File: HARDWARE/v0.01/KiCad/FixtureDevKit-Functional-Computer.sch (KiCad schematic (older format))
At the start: 23 parts, among them J49 Conn_01x20, J50 Conn_01x20, J51 CHIP4RH, J52 Conn_01x35, J53 Conn_01x35, J54 Conn_01x20, J55 Conn_01x20, J56 CHIP4B2B, J57 CHIP4LH, J58 VBUS, J59 USB_A, J60 JST-2P, J61 Audio-Jack-3, SW9 SW_Push

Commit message: updating the cover page
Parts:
- added F?: 3A, symbol Fuse
- added SW?: On/Off, symbol SW_Push_SPDT
- added TP?: D+, symbol TEST
- added TP?: D-, symbol TEST
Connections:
- net USBOTG_B_DM: now also TP?.1
- net USBOTG_B_DP: now also TP?.1
- net C4-PWR-IN: now reaches J55.1 (Pin_1), J57.2 (CHG-IN)
- net C4-PWR-IN: now also J52.31 (Pin_31), J52.32 (Pin_32), J52.33 (Pin_33), J52.34 (Pin_34), J52.35 (Pin_35), J56.61 (USB_VBUS), J56.63 (USB_VBUS), J56.65 (USB_VBUS), J56.67 (USB_VBUS), J56.69 (USB_VBUS), SW?.3 (C)
- net at J51.2 (VCC-5V): no longer J50.1 (Pin_1)
- net I2C-SDA: now reaches J49.18 (Pin_18), J51.35 (GPIODV_28)
- net I2C-SDA: now also J52.29 (Pin_29), J56.57 (GPIODV_28)
- net I2C-SCK: now reaches J49.19 (Pin_19), J51.37 (GPIODV_29)
- net I2C-SCK: now also J52.30 (Pin_30), J56.59 (GPIODV_29)
- net STATUSLED renamed C4-VCC-3V3
- new net: F?.2, SW?.2 (B)
- new net +5V: F?.1
- new net C4-VCC-5V: J50.1 (Pin_1)
- no-connect marks 0 -> 1
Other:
- note added: "PWRSW"
- note added: "Sheet Connections"
- note removed: "TODO:\n- verify all pinouts\n- test points"
- moved on the sheet: J52, J53, J56

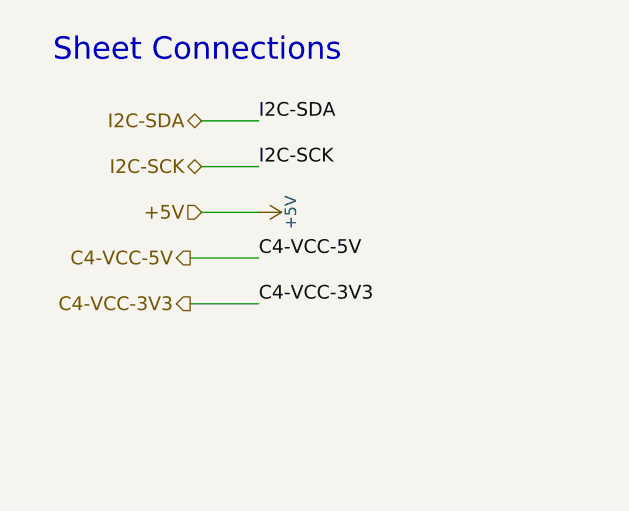
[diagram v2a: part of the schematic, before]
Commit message: adding labelings, hierarchy pins, and page titles
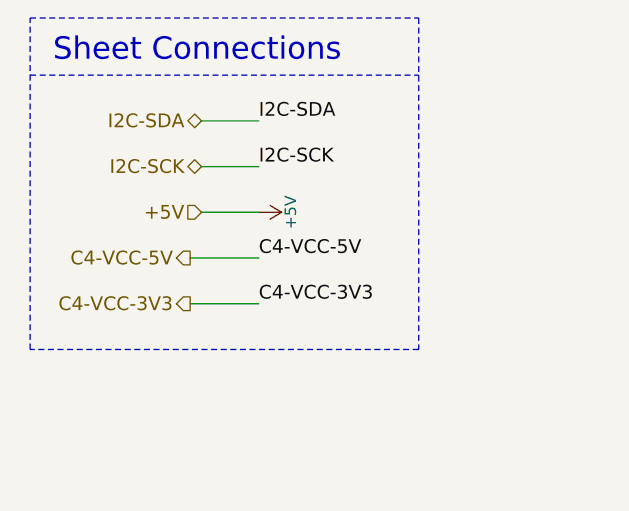
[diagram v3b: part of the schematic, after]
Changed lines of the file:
@@
 encoding utf-8
 Sheet 10 10
-Title ""
-Date ""
-Rev ""
-Comp ""
-Comment1 ""
+Title "CHIP4 Functional Computer"
+Date "2017-10-25"
+Rev "v0.01"
+Comp "Next Thing Co"
+Comment1 "Havin' a Blast!"
 Comment2 ""
 Comment3 ""
@@
 Wire Wire Line
 	9900 950  10100 950
+Wire Notes Line
+	500  500  2200 500
+Wire Notes Line
+	2200 500  2200 1950
+Wire Notes Line
+	2200 1950 500  1950
+Wire Notes Line
+	500  1950 500  500
+Wire Notes Line
+	500  750  2200 750
 $EndSCHEMATC

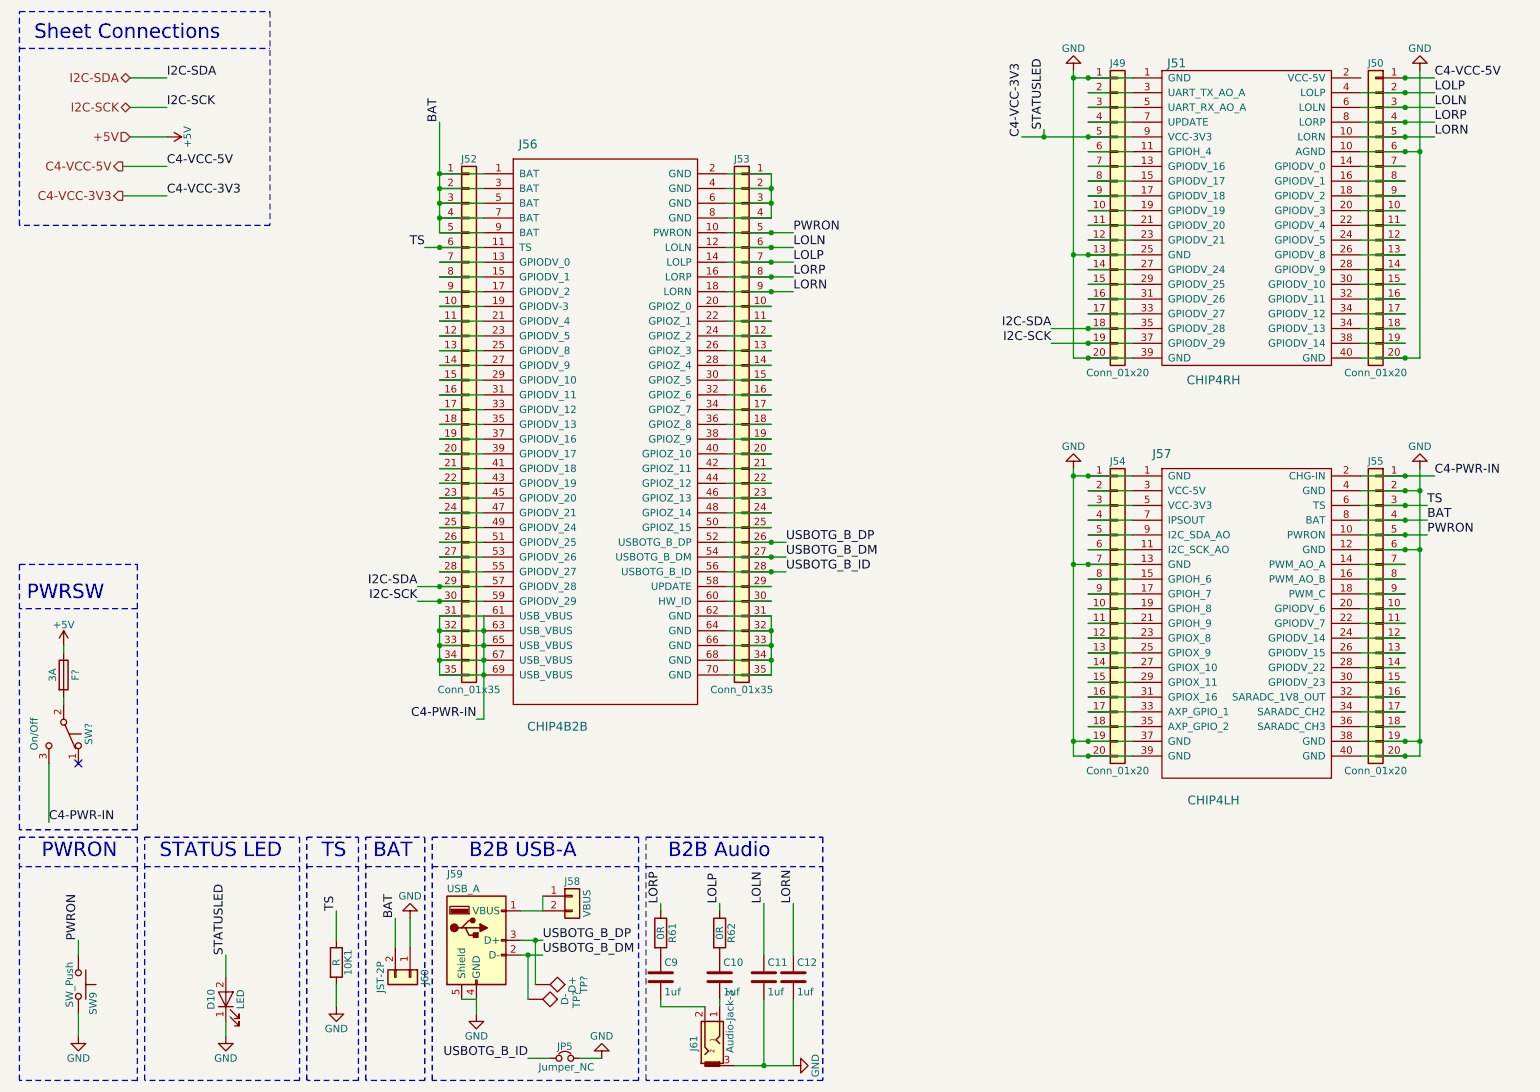
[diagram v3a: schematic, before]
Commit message: adjusting page sizes and cleaning up schematics
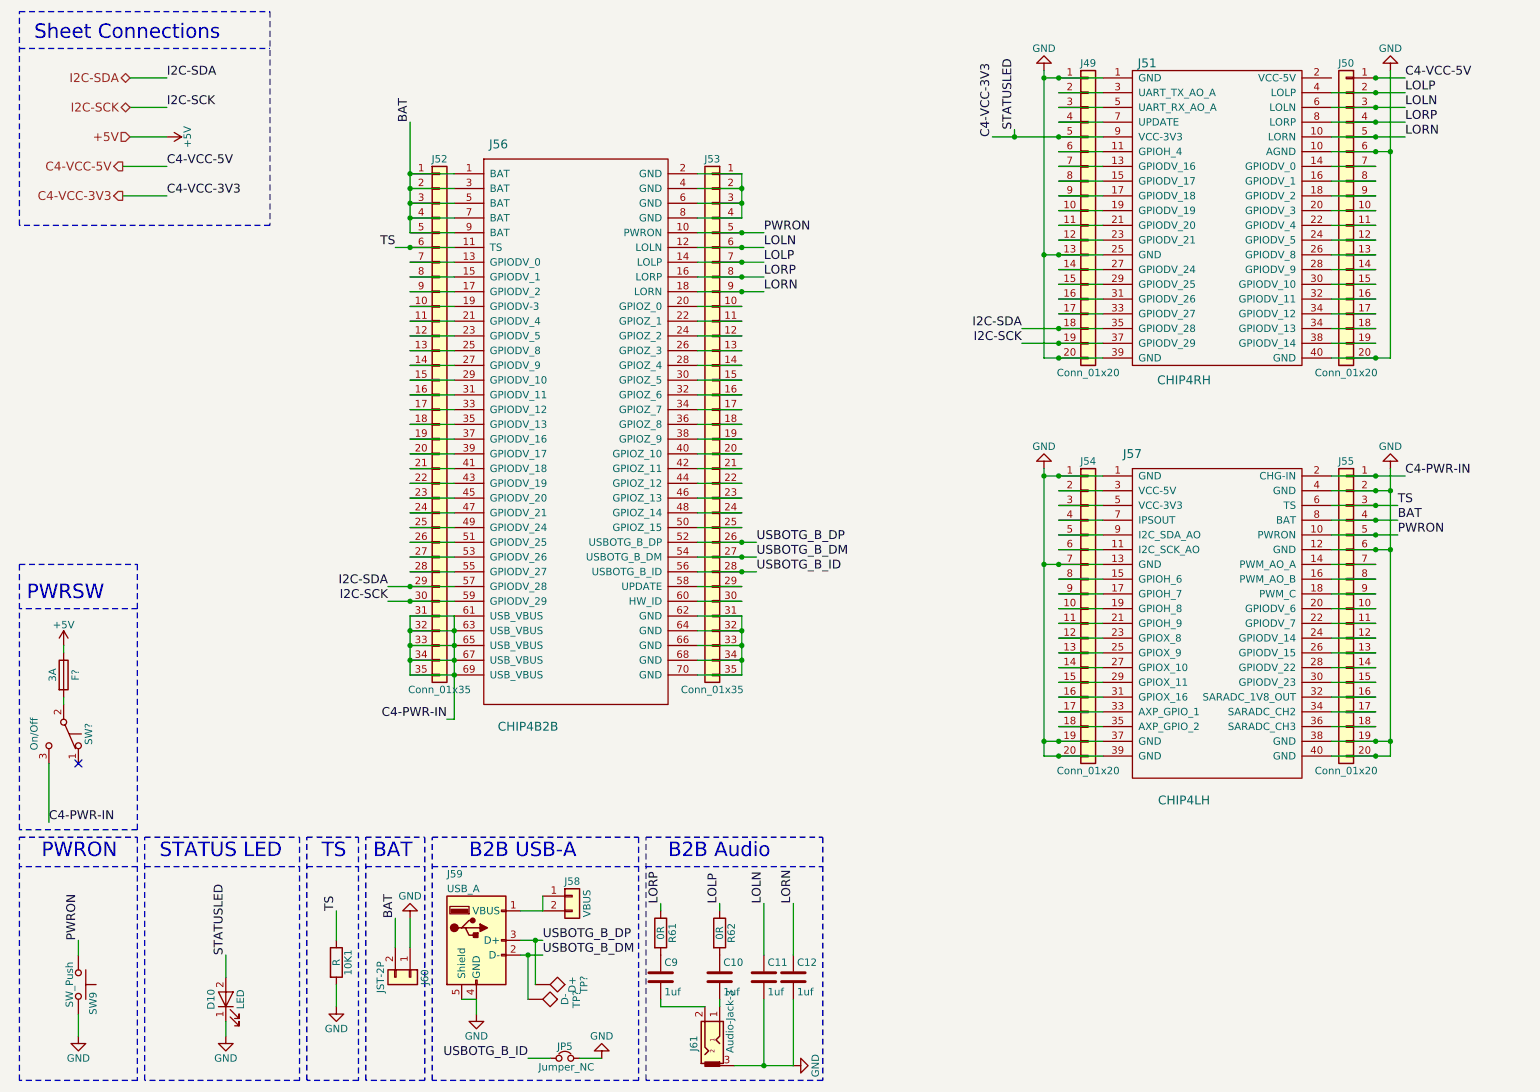
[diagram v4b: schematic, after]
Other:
- moved on the sheet: J49, J50, J51, J52, J53, J54, J55, J56, J57

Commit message: cleaning up schematic, run rules check, generate net list
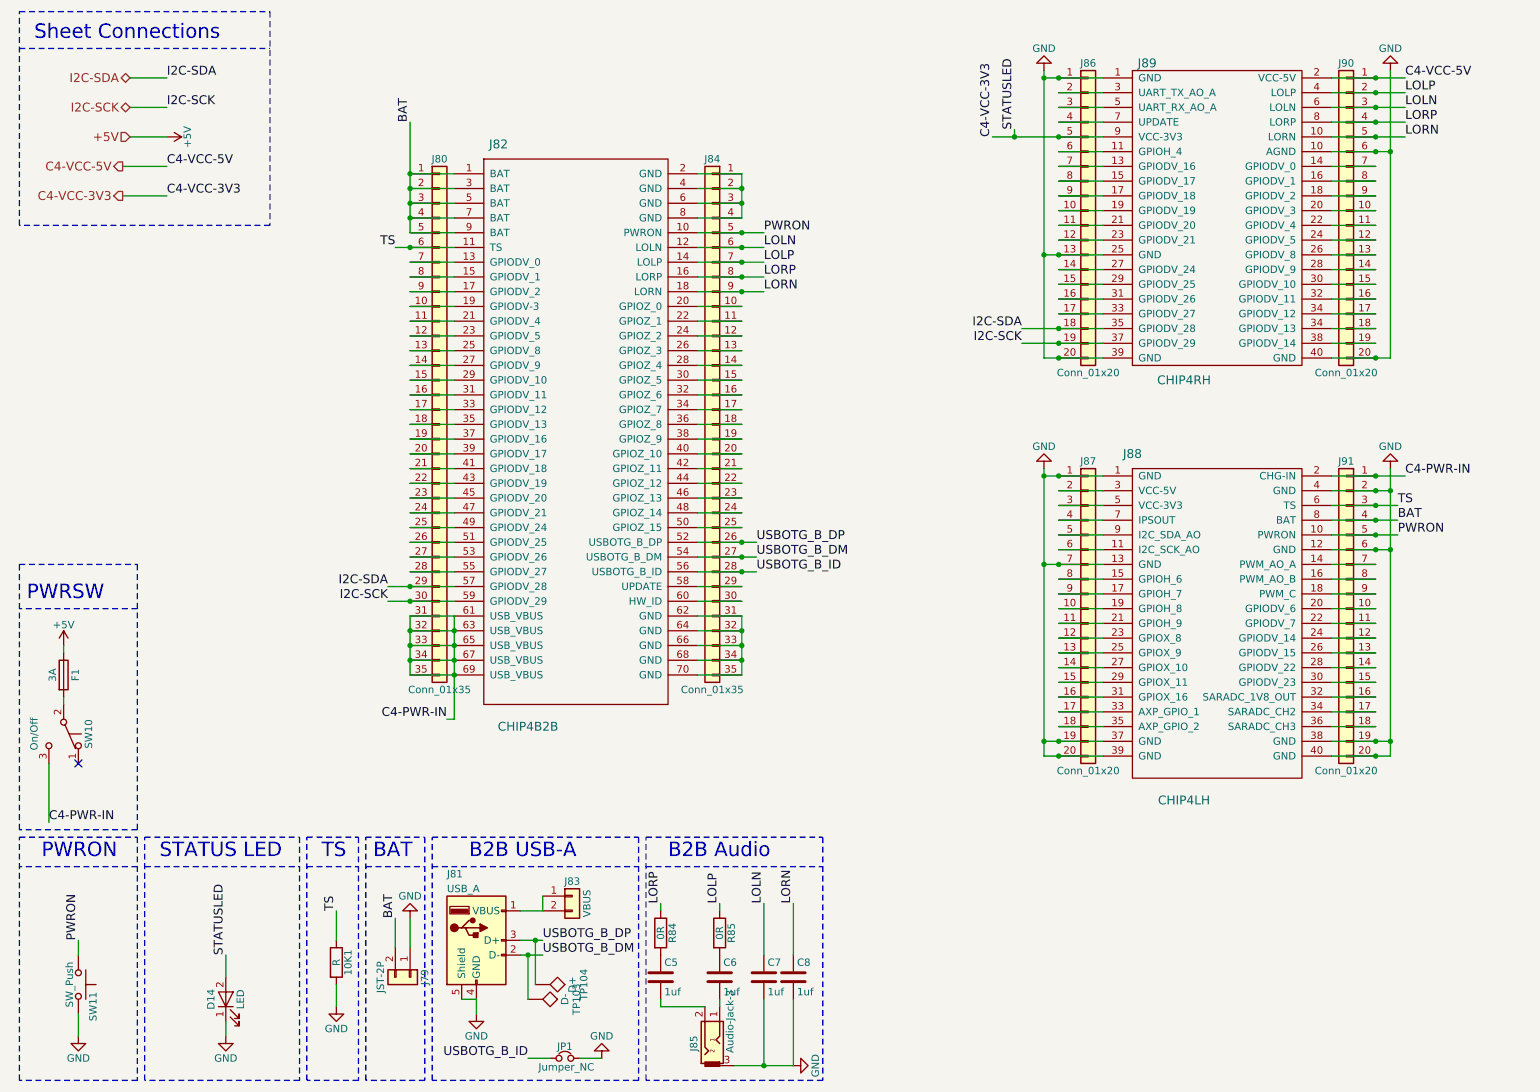
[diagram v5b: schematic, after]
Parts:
- gave numbers to parts that had none: 4
- renumbered C9 to C5, C10 to C6, C11 to C7, C12 to C8, D10 to D14, J60 to J79, J52 to J80, J59 to J81, J56 to J82, J58 to J83, J53 to J84, J61 to J85, J49 to J86, J54 to J87, J57 to J88, J51 to J89, J50 to J90, J55 to J91, JP5 to JP1, R61 to R84, R62 to R85, SW9 to SW11
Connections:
- net C4-VCC-5V: now also J89.2 (VCC-5V)
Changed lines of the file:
@@
 $EndDescr
 $Comp
-L CHIP4LH J57
+L CHIP4LH J88
 U 1 1 59EE680F
 P 8600 5700
-F 0 "J57" H 8050 7900 60  0000 C CNN
+F 0 "J88" H 8050 7900 60  0000 C CNN
 F 1 "CHIP4LH" H 8400 5550 60  0000 C CNN
 F 2 "" H 8700 5700 60  0001 C CNN
@@
 $EndComp
 $Comp
-L CHIP4RH J51
+L CHIP4RH J89
 U 1 1 59EE6892
 P 8650 2900
-F 0 "J51" H 8150 4950 60  0000 C CNN
+F 0 "J89" H 8150 4950 60  0000 C CNN
 F 1 "CHIP4RH" H 8400 2800 60  0000 C CNN
 F 2 "" H 8700 2900 60  0001 C CNN
@@
 $EndComp
 $Comp
-L Conn_01x20 J50
+L Conn_01x20 J90
 U 1 1 59EE69C7
 P 9500 1850
-F 0 "J50" H 9500 2850 50  0000 C CNN
+F 0 "J90" H 9500 2850 50  0000 C CNN
 F 1 "Conn_01x20" H 9500 750 50  0000 C CNN
 F 2 "" H 9500 1850 50  0001 C CNN
@@
 $EndComp
 $Comp
-L Conn_01x20 J49
+L Conn_01x20 J86
 U 1 1 59EE6A17
 P 7750 1850
-F 0 "J49" H 7750 2850 50  0000 C CNN
+F 0 "J86" H 7750 2850 50  0000 C CNN
 F 1 "Conn_01x20" H 7750 750 50  0000 C CNN
 F 2 "" H 7750 1850 50  0001 C CNN
@@
 $EndComp
 $Comp
-L Conn_01x20 J54
+L Conn_01x20 J87
 U 1 1 59EE6A7B
 P 7750 4550
-F 0 "J54" H 7750 5550 50  0000 C CNN
+F 0 "J87" H 7750 5550 50  0000 C CNN
 F 1 "Conn_01x20" H 7750 3450 50  0000 C CNN
 F 2 "" H 7750 4550 50  0001 C CNN
@@
 $EndComp
 $Comp
-L Conn_01x20 J55
+L Conn_01x20 J91
 U 1 1 59EE6B51
 P 9500 4550
-F 0 "J55" H 9500 5550 50  0000 C CNN
+F 0 "J91" H 9500 5550 50  0000 C CNN
 F 1 "Conn_01x20" H 9500 3450 50  0000 C CNN
 F 2 "" H 9500 4550 50  0001 C CNN
@@
 $EndComp
 $Comp
-L GND #PWR048
+L GND #PWR055
 U 1 1 59EE7DE0
 P 7450 900
-F 0 "#PWR048" H 7450 650 50  0001 C CNN
+F 0 "#PWR055" H 7450 650 50  0001 C CNN
 F 1 "GND" H 7450 750 50  0000 C CNN
 F 2 "" H 7450 900 50  0001 C CNN
@@
 $EndComp
 $Comp
-L GND #PWR049
+L GND #PWR056
 U 1 1 59EE7F13
 P 9800 900
-F 0 "#PWR049" H 9800 650 50  0001 C CNN
+F 0 "#PWR056" H 9800 650 50  0001 C CNN
 F 1 "GND" H 9800 750 50  0000 C CNN
 F 2 "" H 9800 900 50  0001 C CNN
@@
 $EndComp
 $Comp
-L GND #PWR050
+L GND #PWR057
 U 1 1 59EE8282
 P 7450 3600
-F 0 "#PWR050" H 7450 3350 50  0001 C CNN
+F 0 "#PWR057" H 7450 3350 50  0001 C CNN
 F 1 "GND" H 7450 3450 50  0000 C CNN
 F 2 "" H 7450 3600 50  0001 C CNN
@@
 $EndComp
 $Comp
-L GND #PWR051
+L GND #PWR058
 U 1 1 59EE829F
 P 9800 3600
-F 0 "#PWR051" H 9800 3350 50  0001 C CNN
+F 0 "#PWR058" H 9800 3350 50  0001 C CNN
 F 1 "GND" H 9800 3450 50  0000 C CNN
 F 2 "" H 9800 3600 50  0001 C CNN
@@
 STATUSLED
 $Comp
-L LED D10
+L LED D14
 U 1 1 59EE94F2
 P 1900 7200
-F 0 "D10" H 1900 7300 50  0000 C CNN
+F 0 "D14" H 1900 7300 50  0000 C CNN
 F 1 "LED" H 1900 7100 50  0000 C CNN
 F 2 "" H 1900 7200 50  0001 C CNN
@@
 $EndComp
 $Comp
-L GND #PWR052
+L GND #PWR059
 U 1 1 59EE95A1
 P 1900 7450
-F 0 "#PWR052" H 1900 7200 50  0001 C CNN
+F 0 "#PWR059" H 1900 7200 50  0001 C CNN
 F 1 "GND" H 1900 7300 50  0000 C CNN
 F 2 "" H 1900 7450 50  0001 C CNN
@@
 PWRON
 $Comp
-L SW_Push SW9
+L SW_Push SW11
 U 1 1 59EEA13E
 P 900 7100
-F 0 "SW9" H 950 7200 50  0000 L CNN
+F 0 "SW11" H 950 7200 50  0000 L CNN
 F 1 "SW_Push" H 900 7040 50  0000 C CNN
 F 2 "" H 900 7300 50  0001 C CNN
@@
 $EndComp
 $Comp
-L GND #PWR053
+L GND #PWR060
 U 1 1 59EEA1C1
 P 900 7450
-F 0 "#PWR053" H 900 7200 50  0001 C CNN
+F 0 "#PWR060" H 900 7200 50  0001 C CNN
 F 1 "GND" H 900 7300 50  0000 C CNN
 F 2 "" H 900 7450 50  0001 C CNN
@@
 $EndComp
 $Comp
-L GND #PWR054
+L GND #PWR061
 U 1 1 59EEADAD
 P 2650 7250
-F 0 "#PWR054" H 2650 7000 50  0001 C CNN
+F 0 "#PWR061" H 2650 7000 50  0001 C CNN
 F 1 "GND" H 2650 7100 50  0000 C CNN
 F 2 "" H 2650 7250 50  0001 C CNN
@@
 BAT
 $Comp
-L GND #PWR055
+L GND #PWR062
 U 1 1 59EEB6E8
 P 3150 6650
-F 0 "#PWR055" H 3150 6400 50  0001 C CNN
+F 0 "#PWR062" H 3150 6400 50  0001 C CNN
 F 1 "GND" H 3150 6500 50  0000 C CNN
 F 2 "" H 3150 6650 50  0001 C CNN
@@
 $EndComp
 $Comp
-L Conn_01x02 J60
+L Conn_01x02 J79
 U 1 1 59EEB707
 P 3150 7050
-F 0 "J60" H 3150 7150 50  0000 C CNN
+F 0 "J79" H 3150 7150 50  0000 C CNN
 F 1 "JST-2P" H 3150 6850 50  0000 C CNN
 F 2 "" H 3150 7050 50  0001 C CNN
@@
 LORN
 $Comp
-L CHIP4B2B J56
+L CHIP4B2B J82
 U 1 1 59EEDA12
 P 4250 5100
-F 0 "J56" H 3750 8800 60  0000 C CNN
+F 0 "J82" H 3750 8800 60  0000 C CNN
 F 1 "CHIP4B2B" H 3950 4850 60  0000 C CNN
 F 2 "" H 4350 6650 60  0001 C CNN
@@
 $EndComp
 $Comp
-L Conn_01x35 J52
+L Conn_01x35 J80
 U 1 1 59EEDDE2
 P 3350 3300
-F 0 "J52" H 3350 5100 50  0000 C CNN
+F 0 "J80" H 3350 5100 50  0000 C CNN
 F 1 "Conn_01x35" H 3350 1500 50  0000 C CNN
 F 2 "" H 3350 3300 50  0001 C CNN
@@
 $EndComp
 $Comp
-L Conn_01x35 J53
+L Conn_01x35 J84
 U 1 1 59EEDE6B
 P 5200 3300
-F 0 "J53" H 5200 5100 50  0000 C CNN
+F 0 "J84" H 5200 5100 50  0000 C CNN
 F 1 "Conn_01x35" H 5200 1500 50  0000 C CNN
 F 2 "" H 5200 3300 50  0001 C CNN
@@
 USBOTG_B_ID
 $Comp
-L GND #PWR056
+L GND #PWR063
 U 1 1 59EF55B6
 P 3600 7300
-F 0 "#PWR056" H 3600 7050 50  0001 C CNN
+F 0 "#PWR063" H 3600 7050 50  0001 C CNN
 F 1 "GND" H 3600 7150 50  0000 C CNN
 F 2 "" H 3600 7300 50  0001 C CNN
@@
 $EndComp
 $Comp
-L Jumper_NC_Small JP5
+L Jumper_NC_Small JP1
 U 1 1 59EF5E24
 P 4200 7600
-F 0 "JP5" H 4200 7680 50  0000 C CNN
+F 0 "JP1" H 4200 7680 50  0000 C CNN
 F 1 "Jumper_NC" H 4210 7540 50  0000 C CNN
 F 2 "" H 4200 7600 50  0001 C CNN
@@
 $EndComp
 $Comp
-L GND #PWR057
+L GND #PWR064
 U 1 1 59EF61DC
 P 4450 7600
-F 0 "#PWR057" H 4450 7350 50  0001 C CNN
+F 0 "#PWR064" H 4450 7350 50  0001 C CNN
 F 1 "GND" H 4450 7450 50  0000 C CNN
 F 2 "" H 4450 7600 50  0001 C CNN
@@
 USBOTG_B_DP
 $Comp
-L USB_A J59
+L USB_A J81
 U 1 1 59EF4A5C
 P 3600 6800
-F 0 "J59" H 3400 7250 50  0000 L CNN
+F 0 "J81" H 3400 7250 50  0000 L CNN
 F 1 "USB_A" H 3400 7150 50  0000 L CNN
 F 2 "" H 3750 6750 50  0001 C CNN
@@
 $EndComp
 $Comp
-L Conn_01x02 J58
+L Conn_01x02 J83
 U 1 1 59F0CB92
 P 4250 6500
-F 0 "J58" H 4250 6600 50  0000 C CNN
+F 0 "J83" H 4250 6600 50  0000 C CNN
 F 1 "VBUS" V 4350 6450 50  0000 C CNN
 F 2 "" H 4250 6500 50  0001 C CNN
@@
 $EndComp
 $Comp
-L Audio-Jack-3 J61
+L Audio-Jack-3 J85
 U 1 1 59F0D2AB
 P 5250 7450
-F 0 "J61" H 5200 7625 50  0000 C CNN
+F 0 "J85" H 5200 7625 50  0000 C CNN
 F 1 "Audio-Jack-3" H 5350 7380 50  0000 C CNN
 F 2 "" H 5500 7550 50  0001 C CNN
@@
 LORN
 $Comp
-L R R61
+L R R84
 U 1 1 59F0D645
 P 4850 6750
-F 0 "R61" V 4930 6750 50  0000 C CNN
+F 0 "R84" V 4930 6750 50  0000 C CNN
 F 1 "0R" V 4850 6750 50  0000 C CNN
 F 2 "" V 4780 6750 50  0001 C CNN
@@
 $EndComp
 $Comp
-L C C9
+L C C5
 U 1 1 59F0D690
 P 4850 7050
-F 0 "C9" H 4875 7150 50  0000 L CNN
+F 0 "C5" H 4875 7150 50  0000 L CNN
 F 1 "1uf" H 4875 6950 50  0000 L CNN
 F 2 "" H 4888 6900 50  0001 C CNN
@@
 $EndComp
 $Comp
-L R R62
+L R R85
 U 1 1 59F0DD42
 P 5250 6750
-F 0 "R62" V 5330 6750 50  0000 C CNN
+F 0 "R85" V 5330 6750 50  0000 C CNN
 F 1 "0R" V 5250 6750 50  0000 C CNN
 F 2 "" V 5180 6750 50  0001 C CNN
@@
 $EndComp
 $Comp
-L C C10
+L C C6
 U 1 1 59F0DD9A
 P 5250 7050
-F 0 "C10" H 5275 7150 50  0000 L CNN
+F 0 "C6" H 5275 7150 50  0000 L CNN
 F 1 "1uf" H 5275 6950 50  0000 L CNN
 F 2 "" H 5288 6900 50  0001 C CNN
@@
 LOLP
 $Comp
-L C C11
+L C C7
 U 1 1 59F0E267
 P 5550 7050
-F 0 "C11" H 5575 7150 50  0000 L CNN
+F 0 "C7" H 5575 7150 50  0000 L CNN
 F 1 "1uf" H 5575 6950 50  0000 L CNN
 F 2 "" H 5588 6900 50  0001 C CNN
@@
 $EndComp
 $Comp
-L C C12
+L C C8
 U 1 1 59F0E2C1
 P 5750 7050
-F 0 "C12" H 5775 7150 50  0000 L CNN
+F 0 "C8" H 5775 7150 50  0000 L CNN
 F 1 "1uf" H 5775 6950 50  0000 L CNN
 F 2 "" H 5788 6900 50  0001 C CNN
@@
 $EndComp
 $Comp
-L GND #PWR058
+L GND #PWR065
 U 1 1 59F0E393
 P 5750 7650
-F 0 "#PWR058" H 5750 7400 50  0001 C CNN
+F 0 "#PWR065" H 5750 7400 50  0001 C CNN
 F 1 "GND" H 5750 7500 50  0000 C CNN
 F 2 "" H 5750 7650 50  0001 C CNN
@@
 Sheet Connections
 $Comp
-L +5V #PWR?
+L +5V #PWR066
 U 1 1 59F1E155
 P 1500 1350
-F 0 "#PWR?" H 1500 1200 50  0001 C CNN
+F 0 "#PWR066" H 1500 1200 50  0001 C CNN
 F 1 "+5V" H 1500 1490 50  0000 C CNN
 F 2 "" H 1500 1350 50  0001 C CNN
@@
 +5V
 $Comp
-L +5V #PWR?
+L +5V #PWR067
 U 1 1 59F1EC3F
 P 800 4800
-F 0 "#PWR?" H 800 4650 50  0001 C CNN
+F 0 "#PWR067" H 800 4650 50  0001 C CNN
 F 1 "+5V" H 800 4940 50  0000 C CNN
 F 2 "" H 800 4800 50  0001 C CNN
@@
 $EndComp
 $Comp
-L Fuse F?
+L Fuse F1
 U 1 1 59F1EC7A
 P 800 5000
-F 0 "F?" V 880 5000 50  0000 C CNN
+F 0 "F1" V 880 5000 50  0000 C CNN
 F 1 "3A" V 725 5000 50  0000 C CNN
 F 2 "" V 730 5000 50  0001 C CNN
@@
 $EndComp
 $Comp
-L SW_Push_SPDT SW?
+L SW_Push_SPDT SW10
 U 1 1 59F1EDC7
 P 800 5400
-F 0 "SW?" H 800 5570 50  0000 C CNN
+F 0 "SW10" H 800 5570 50  0000 C CNN
 F 1 "On/Off" H 800 5200 50  0000 C CNN
 F 2 "" H 800 5400 50  0001 C CNN
@@
 C4-PWR-IN
 $Comp
-L TEST TP?
+L TEST TP104
 U 1 1 59F2229B
 P 4000 7100
-F 0 "TP?" H 4000 7400 50  0000 C BNN
+F 0 "TP104" H 4000 7400 50  0000 C BNN
 F 1 "D+" H 4000 7350 50  0000 C CNN
 F 2 "" H 4000 7100 50  0001 C CNN
@@
 $EndComp
 $Comp
-L TEST TP?
+L TEST TP103
 U 1 1 59F223B8
 P 3950 7200
-F 0 "TP?" H 3950 7500 50  0000 C BNN
+F 0 "TP103" H 3950 7500 50  0000 C BNN
 F 1 "D-" H 3950 7450 50  0000 C CNN
 F 2 "" H 3950 7200 50  0001 C CNN
@@
 C4-VCC-5V
 Wire Wire Line
-	9700 950  9900 950
+	9400 950  9900 950
 Wire Notes Line
 	500  500  2200 500
